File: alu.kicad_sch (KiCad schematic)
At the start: 23 parts, among them SW1 SW_DIP_x04, SW2 SW_DIP_x04, SW3 SW_DIP_x04, U1 74HC138

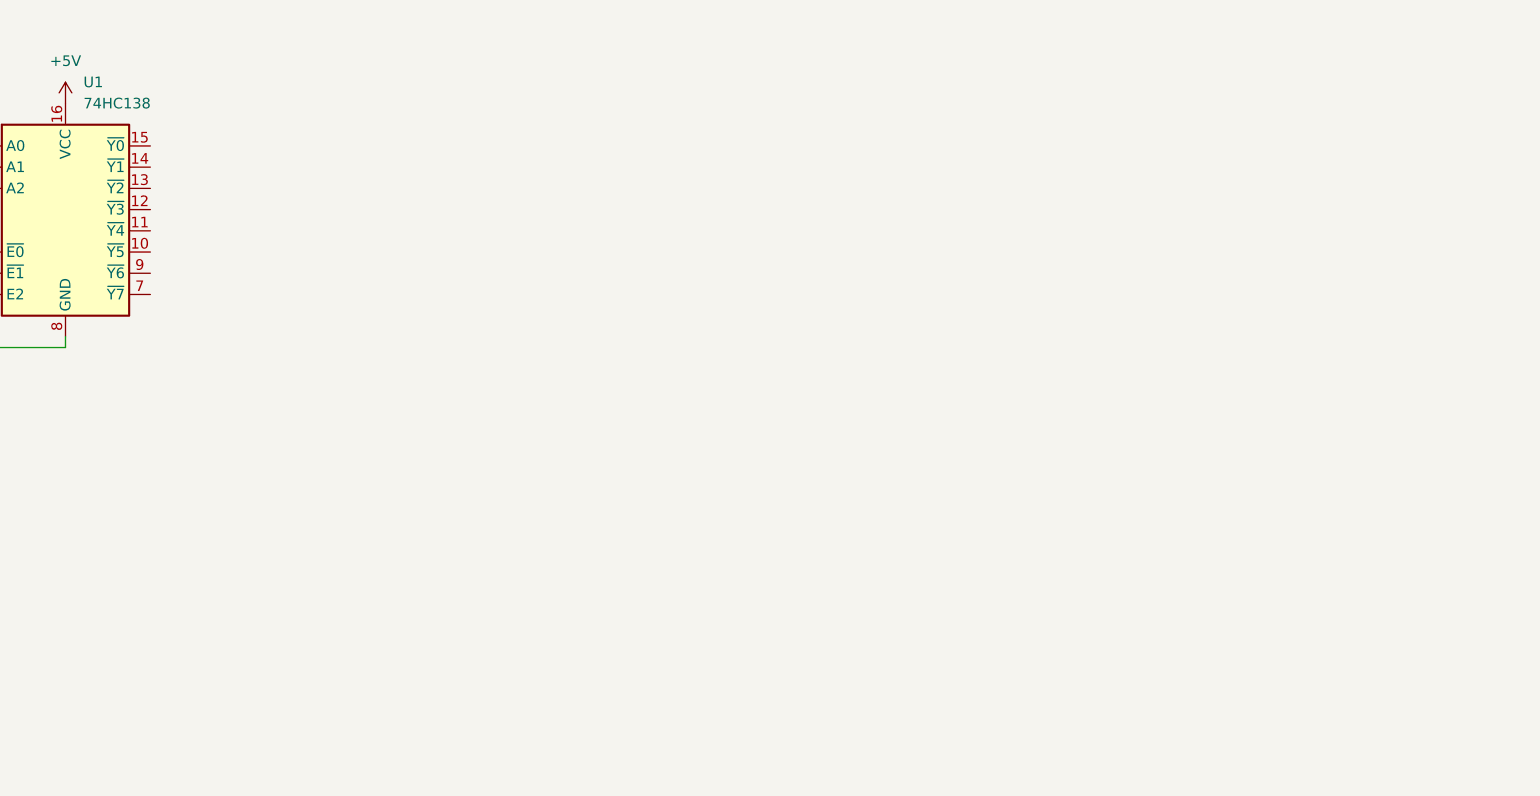
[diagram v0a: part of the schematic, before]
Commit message: feat: 4-bit adder
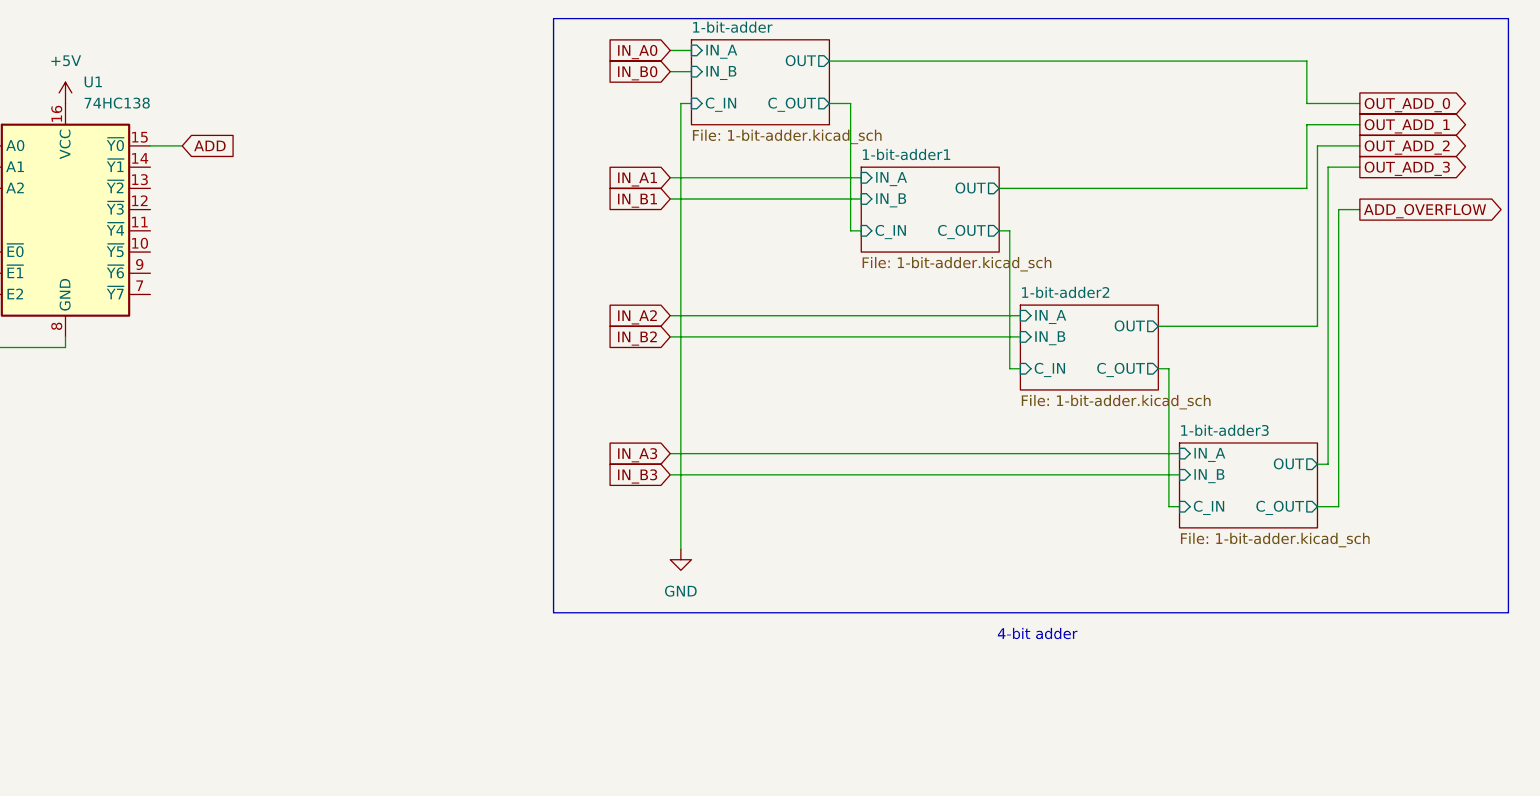
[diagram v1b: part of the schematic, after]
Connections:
- net ADD: now reaches U1.15 (~{Y0})
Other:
- added sheet 1-bit-adder (1-bit-adder.kicad_sch)
- added sheet 1-bit-adder1 (1-bit-adder.kicad_sch)
- added sheet 1-bit-adder2 (1-bit-adder.kicad_sch)
- added sheet 1-bit-adder3 (1-bit-adder.kicad_sch)
- note added: "4-bit adder"

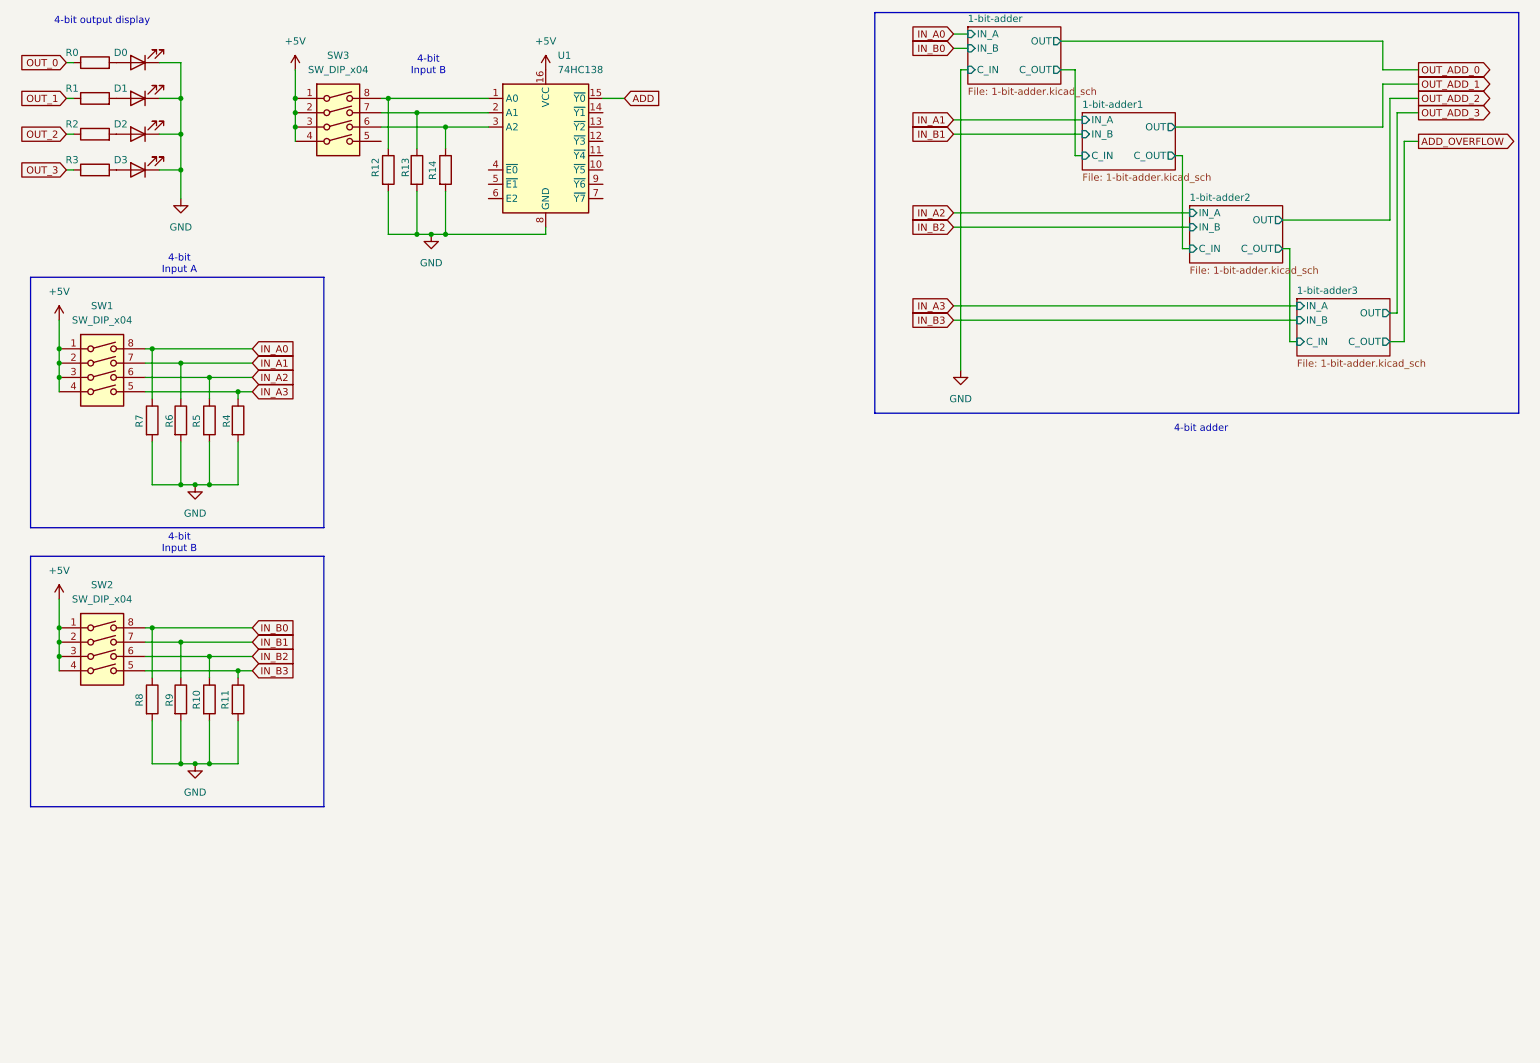
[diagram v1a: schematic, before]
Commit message: feat: working 4-bit adder (normally)
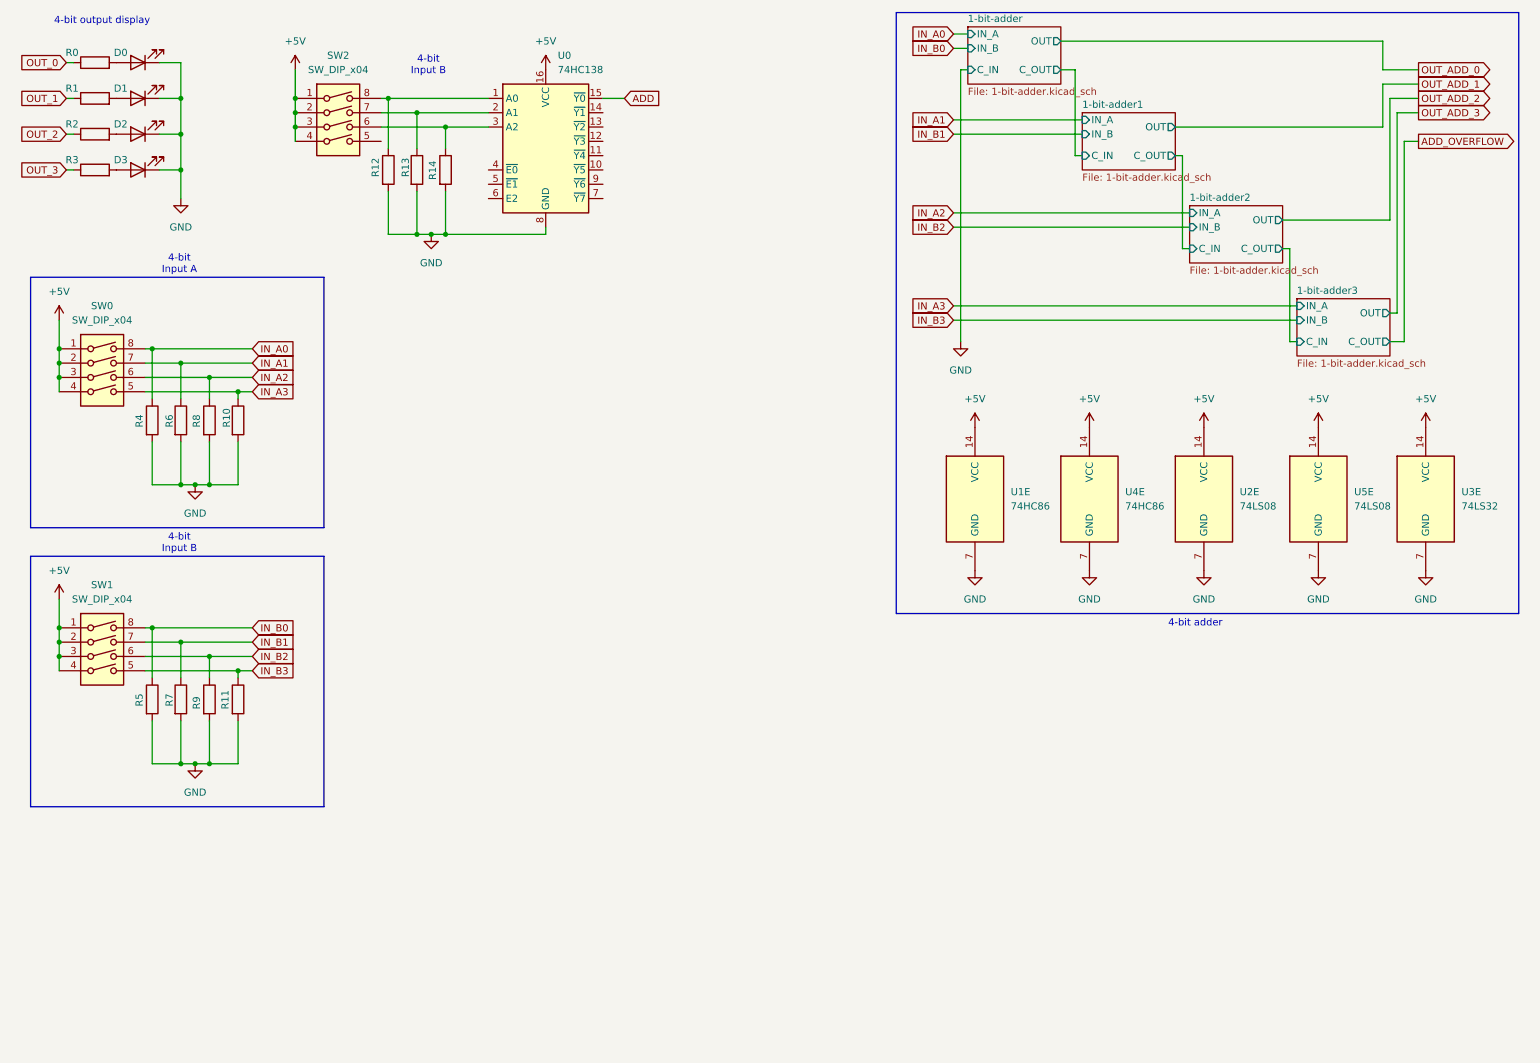
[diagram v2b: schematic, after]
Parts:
- added U1, U4: 74HC86, symbol 74xx:74HC86
- added U2, U5: 74LS08, symbol 74xx:74LS08
- added U3: 74LS32, symbol 74xx:74LS32
- renumbered R4 to R10, R7 to R4, R8 to R5, R9 to R7, R5 to R8, R10 to R9, SW1 to SW0, SW2 to SW1, SW3 to SW2, U1 to U0
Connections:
- net +5V: now also U1.14 (VCC), U2.14 (VCC), U3.14 (VCC), U4.14 (VCC), U5.14 (VCC)
- net GND: now also U1.7 (GND), U2.7 (GND), U3.7 (GND), U4.7 (GND), U5.7 (GND)

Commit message: feat: mul
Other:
- added sheet 2-bit-mul (2-bit-mul.kicad_sch)
- note added: "4-bit mul"
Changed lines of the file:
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@@
 	)
 	(rectangle
+		(start 77.47 156.21)
+		(end 167.64 191.77)
+		(stroke
+			(width 0)
+			(type default)
+		)
+		(fill
+			(type none)
+		)
+	)
+	(rectangle
 		(start 20.32 59.69)
 		(end 72.39 104.14)
@@
 		)
 	)
+	(text "4-bit mul"
+		(exclude_from_sim no)
+		(at 124.206 196.088 0)
+		(effects
+			(font
+				(size 1.27 1.27)
+			)
+		)
+	)
 	(text "4-bit \nInput B"
 		(exclude_from_sim no)
@@
 				)
 			)
+		)
+	)
+	(sheet
+		(at 81.28 161.29)
+		(size 22.86 12.7)
+		(exclude_from_sim no)
+		(in_bom yes)
+		(on_board yes)
+		(dnp no)
+		(fields_autoplaced yes)
+		(stroke
+			(width 0.1524)
+			(type solid)
+		)
+		(fill
+			(color 0 0 0 0.0000)
+		)
+		(property "Sheetname" "2-bit-mul"
+			(at 81.28 160.5784 0)
+			(show_name yes)
+			(effects
+				(font
+					(size 1.27 1.27)
+				)
+				(justify left bottom)
+			)
+		)
+		(property "Sheetfile" "2-bit-mul.kicad_sch"
+			(at 81.28 174.5746 0)
+			(effects
+				(font
+					(size 1.27 1.27)
+				)
+				(justify left top)
+			)
+		)
+		(instances
+			(project "alu"
+				(path "/4987240f-8890-46b8-b8e9-0d60580cb205"
+					(page "6")
+				)
+			)

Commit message: feat(mul): clean version
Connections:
- net MUL: now reaches U0.13 (~{Y2})
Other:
- sheet 2-bit-mul ports: added IN_A0, IN_A1, IN_B0, IN_B1, OUT_MUL_0, OUT_MUL_1, OUT_MUL_2, OUT_MUL_3; removed none
